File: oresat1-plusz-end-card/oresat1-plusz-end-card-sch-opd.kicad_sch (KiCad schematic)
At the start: 68 parts, among them Q1 DMP2240UDM-7, Q11 DMP2240UDM-7, Q2 DMN3028LQ-7, Q3 DMN3028LQ-7, Q4 DMN3028LQ-7, Q6 DMN3028LQ-7, Q9 DMP2240UDM-7, U11 MIC842LYC5, U12 MIC842LYC5, U2 MAX7310, U201 TS5A21366, U203 TS5A21366, U204 TS5A21366, U205 TS5A21366

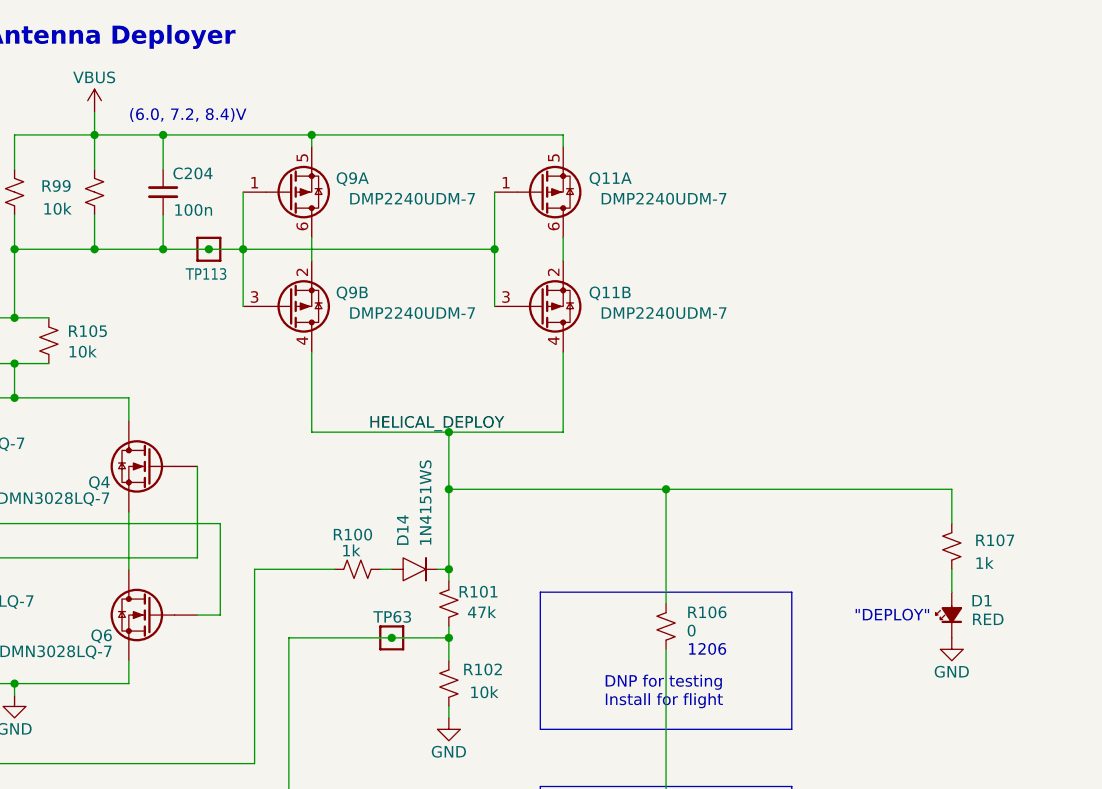
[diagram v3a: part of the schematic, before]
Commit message: Last minute polishing; lost a custom capacitor, and better ground stiching
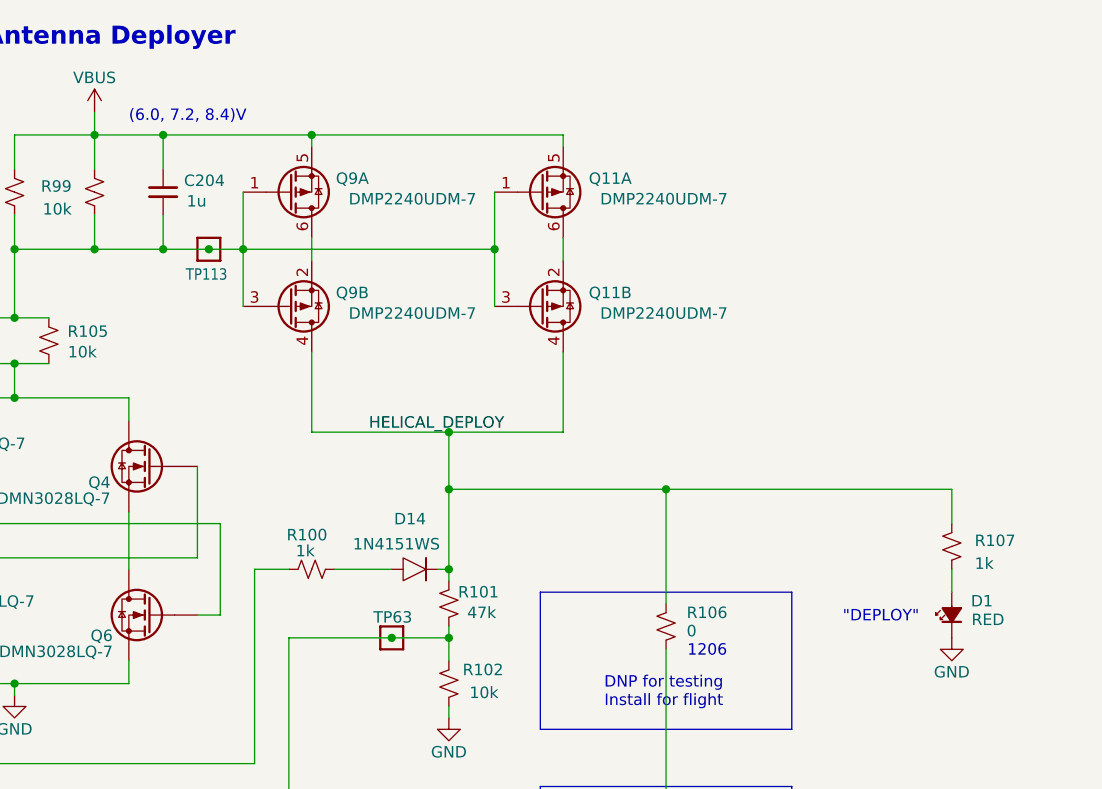
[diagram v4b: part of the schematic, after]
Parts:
- C204: value 100n -> 1u; DPN 399-6856-1-ND -> 490-GRT188R71E105KE13DCT-ND; MFR KEMET -> Murata Electronics; MPN C0603C104K5RACAUTO -> GRT188R71E105KE13D
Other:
- moved on the sheet: R100
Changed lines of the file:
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@@
 	(text "\"DEPLOY\""
 		(exclude_from_sim no)
-		(at 356.616 103.124 0)
+		(at 355.346 103.124 0)
 		(effects
 			(font
@@
 	(wire
 		(pts
-			(xy 299.72 97.79) (xy 300.99 97.79)
+			(xy 294.64 97.79) (xy 300.99 97.79)
 		)
 		(stroke
@@
 	(wire
 		(pts
-			(xy 285.75 97.79) (xy 294.64 97.79)
+			(xy 285.75 97.79) (xy 289.56 97.79)
 		)
 		(stroke
@@
 		(dnp no)
 		(property "Reference" "D14"
-			(at 302.26 95.25 90)
+			(at 301.244 92.202 0)
 			(show_name no)
 			(do_not_autoplace no)
@@
 		)
 		(property "Value" "1N4151WS"
-			(at 304.8 95.25 90)
+			(at 296.672 94.996 0)
 			(show_name no)
 			(do_not_autoplace no)
@@
 	(symbol
 		(lib_id "Device:R_Small_US")
-		(at 297.18 97.79 90)
+		(at 292.1 97.79 90)
 		(unit 1)
 		(body_style 1)
@@
 		(dnp no)
 		(property "Reference" "R100"
-			(at 294.386 93.98 90)
+			(at 289.306 93.98 90)
 			(show_name no)
 			(do_not_autoplace no)
@@
 		)
 		(property "Value" "1k"
-			(at 295.402 95.758 90)
+			(at 290.322 95.758 90)
 			(show_name no)
 			(do_not_autoplace no)
@@
 		)
 		(property "Footprint" "oresat-passives:0603-C-NOSILK"
-			(at 297.18 97.79 0)
+			(at 292.1 97.79 0)
 			(hide yes)
 			(show_name no)
@@
 		)
 		(property "Datasheet" "https://www.seielect.com/catalog/SEI-RMCF_RMCP.pdf"
-			(at 297.18 97.79 0)
+			(at 292.1 97.79 0)
 			(hide yes)
 			(show_name no)
@@
 		)
 		(property "Description" "1 kOhms ±1% 0.1W, 1/10W Chip Resistor 0603 (1608 Metric) Automotive AEC-Q200 Thick Film"
-			(at 297.18 97.79 0)
+			(at 292.1 97.79 0)
 			(hide yes)
 			(show_name no)
@@
 		)
 		(property "DPN" "RMCF0603FT1K00CT-ND"
-			(at 297.18 97.79 0)
+			(at 292.1 97.79 0)
 			(hide yes)
 			(show_name no)
@@
 		)
 		(property "MFR" "Stackpole Electronics Inc"
-			(at 297.18 97.79 0)
+			(at 292.1 97.79 0)
 			(hide yes)
 			(show_name no)
@@
 		)
 		(property "MPN" "RMCF0603FT1K00"
-			(at 297.18 97.79 0)
+			(at 292.1 97.79 0)
 			(hide yes)
 			(show_name no)
@@
 		)
 		(property "DIS" "DigiKey"
-			(at 297.18 97.79 0)
+			(at 292.1 97.79 0)
 			(hide yes)
 			(show_name no)
@@
 		)
 		(property "Value_1" ""
-			(at 297.18 97.79 0)
+			(at 292.1 97.79 0)
 			(hide yes)
 			(show_name no)
@@
 		(dnp no)
 		(property "Reference" "C204"
-			(at 281.178 53.848 0)
+			(at 282.448 54.61 0)
 			(show_name no)
 			(do_not_autoplace no)
@@
 			)
 		)
-		(property "Value" "100n"
-			(at 281.178 57.912 0)
+		(property "Value" "1u"
+			(at 280.416 56.896 0)
 			(show_name no)
 			(do_not_autoplace no)
@@
 			)
 		)
-		(property "Datasheet" "https://search.kemet.com/download/specsheet/C0603C104K5RACAUTO"
+		(property "Datasheet" "https://search.murata.co.jp/Ceramy/image/img/A01X/G101/ENG/GRT188R71E105KE13-01.pdf"
 			(at 275.59 55.88 0)
 			(hide yes)
@@
 			)
 		)
-		(property "Description" "0.1 µF ±10% 50V Ceramic Capacitor X7R 0603 (1608 Metric)"
+		(property "Description" "1 µF ±10% 25V Ceramic Capacitor X7R 0603 (1608 Metric)"
 			(at 275.59 55.88 0)
 			(hide yes)
@@
 			)
 		)
-		(property "DPN" "399-6856-1-ND"
+		(property "DPN" "490-GRT188R71E105KE13DCT-ND"
 			(at 275.59 55.88 0)
 			(hide yes)
@@
 			)
 		)
-		(property "MFR" "KEMET"
+		(property "MFR" "Murata Electronics"
 			(at 275.59 55.88 0)
 			(hide yes)
@@
 			)
 		)
-		(property "MPN" "C0603C104K5RACAUTO"
+		(property "MPN" "GRT188R71E105KE13D"
 			(at 275.59 55.88 0)
 			(hide yes)
